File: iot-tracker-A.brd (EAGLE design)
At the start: 21.6 x 19.6 mm, 23 parts, among them U1 ESP-WROOM-02, U2 TPL5111DDCR, U3 TPS61021ADSGR

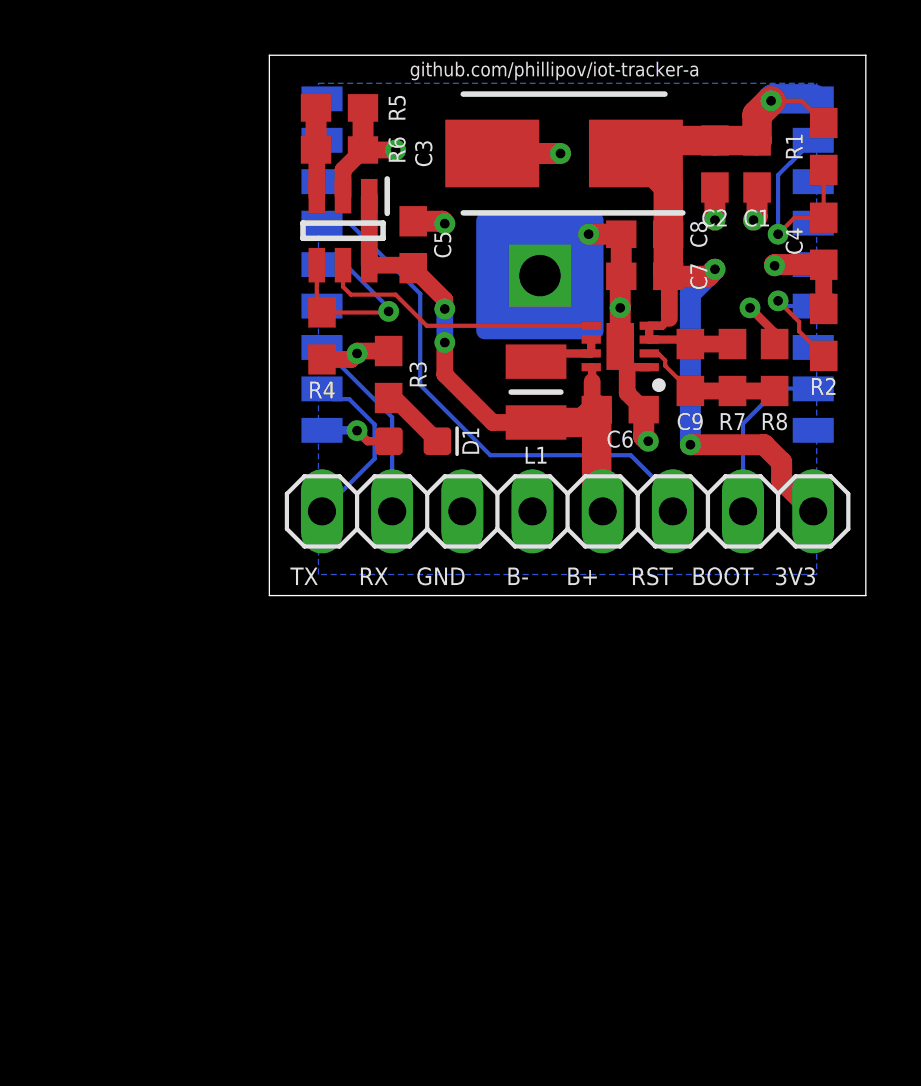
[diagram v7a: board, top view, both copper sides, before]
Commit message: Started integrating the RTC
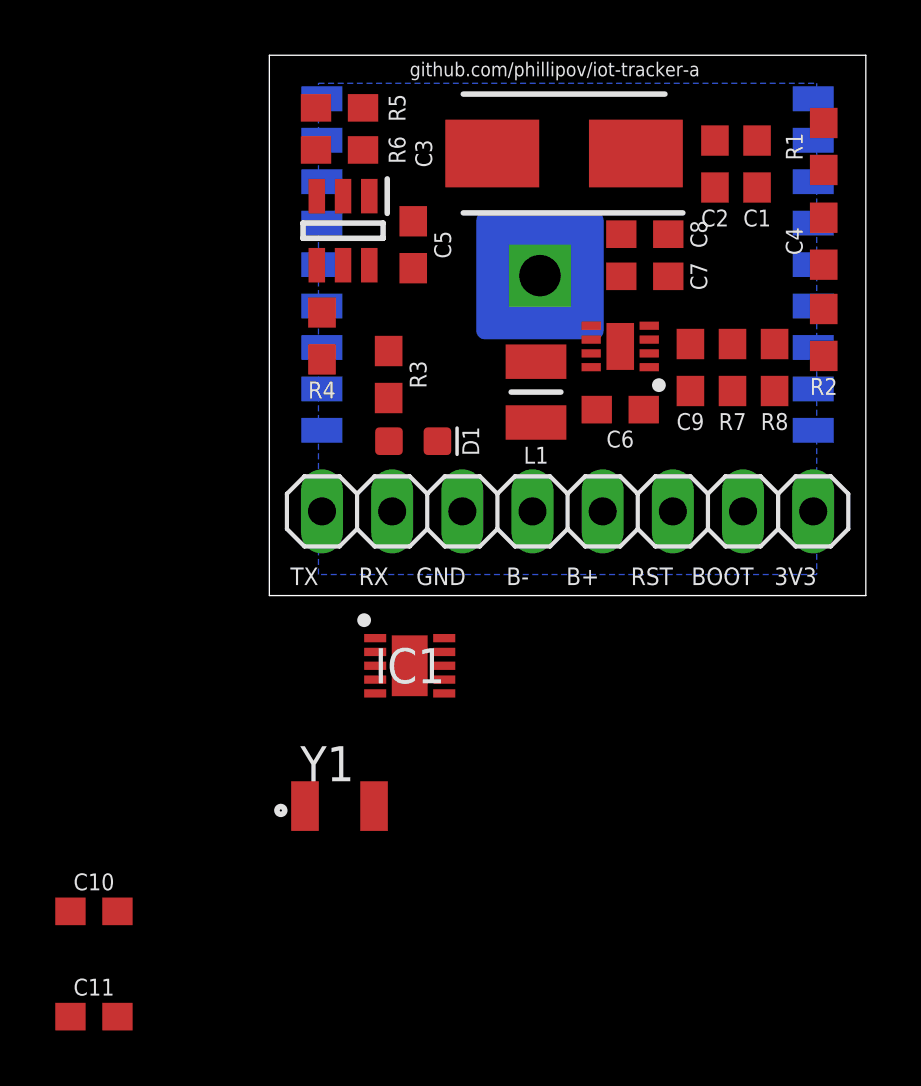
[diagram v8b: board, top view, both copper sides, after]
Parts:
- added C10, C11: 0.1uF, SparkFun-Capacitors:0603
- added IC1: PCF85263ATL_AX, IOT-Tracker-A:SON50P260X260X50-11N
- added Y1: FC-135_32.7680KA-AG3, IOT-Tracker-A:FC-135_1
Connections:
- new net OSCI: IC1.1, Y1.1
- new net OSCO: IC1.2, Y1.2
- net 3.3V: now also C11.2, IC1.10
- net GND: now also C10.1, C11.1, IC1.5
- net V_BATT: now also C10.2, IC1.3
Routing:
- net 3.3V: track 35.2 -> 0.00 mm, vias 3 -> 0
- net GND: track 28.0 -> 0.00 mm, vias 11 -> 0
- net V_BATT: track 20.3 -> 0.00 mm, vias 2 -> 0
- net RST: track 19.3 -> 0.00 mm
- net DRVN: track 10.3 -> 0.00 mm
- net EN: track 7.56 -> 0.00 mm, vias 1 -> 0
- net DONE: track 7.41 -> 0.00 mm, vias 1 -> 0
- net TX: track 7.00 -> 0.00 mm
- net RX: track 6.37 -> 0.00 mm
- net BOOT: track 6.25 -> 0.00 mm
- net FB: track 5.22 -> 0.00 mm
- net IO15: track 4.03 -> 0.00 mm, vias 1 -> 0
- net DELAY: track 3.21 -> 0.00 mm
- net SW: track 2.62 -> 0.00 mm
- net IO4_LED: track 2.59 -> 0.00 mm, vias 1 -> 0
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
